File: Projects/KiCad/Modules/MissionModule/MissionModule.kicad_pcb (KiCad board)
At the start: 2 copper layers, 110 x 95 mm, 55 parts, among them J1 Conn_01x08, J2 Micro_SD_Card_Det_Hirose_DM3AT, SW1 SW_DIP_x02, U1 MCP2562-E-P, U2 MCP2515-I/P, U3 NJM7805SDL1, U5 TLP222A, U6 ABX00012, U7 MB85RS2MT, U8 MB85RS2MT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

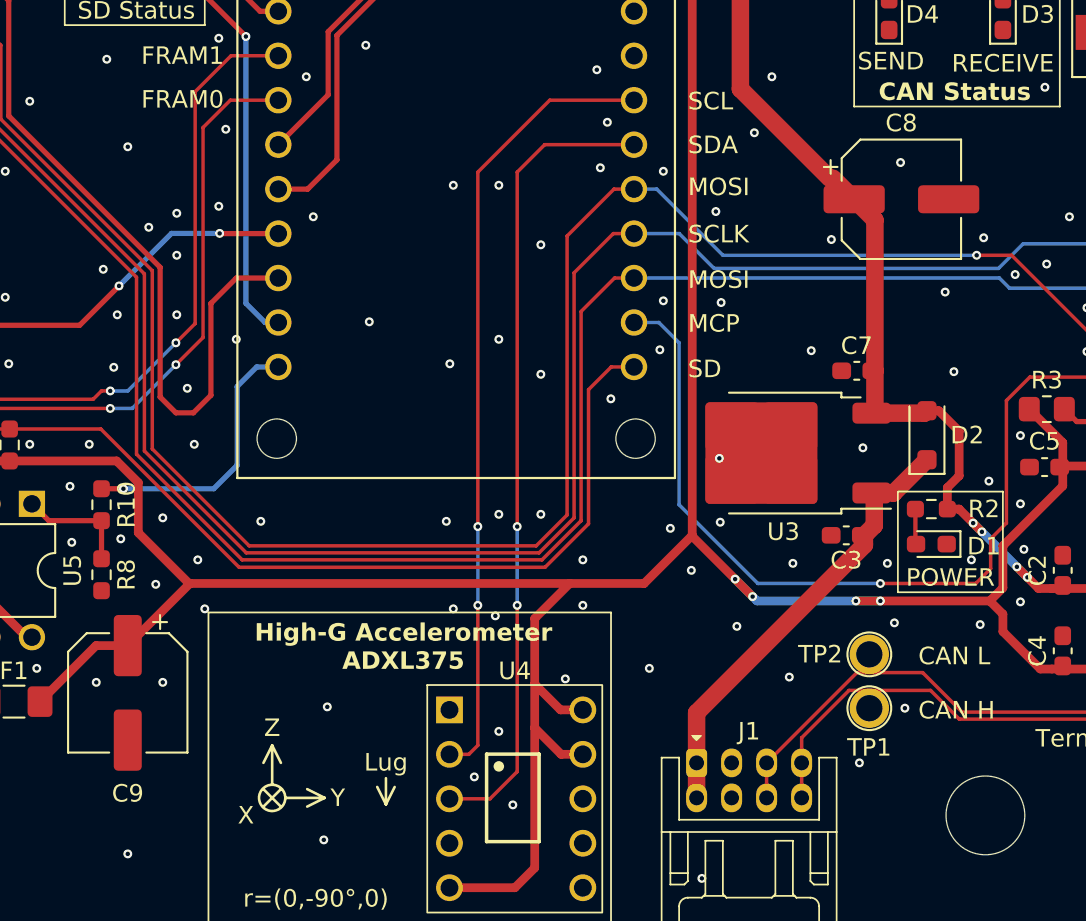
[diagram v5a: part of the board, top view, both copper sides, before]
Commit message: バッファコンデンサを表面実装に変更
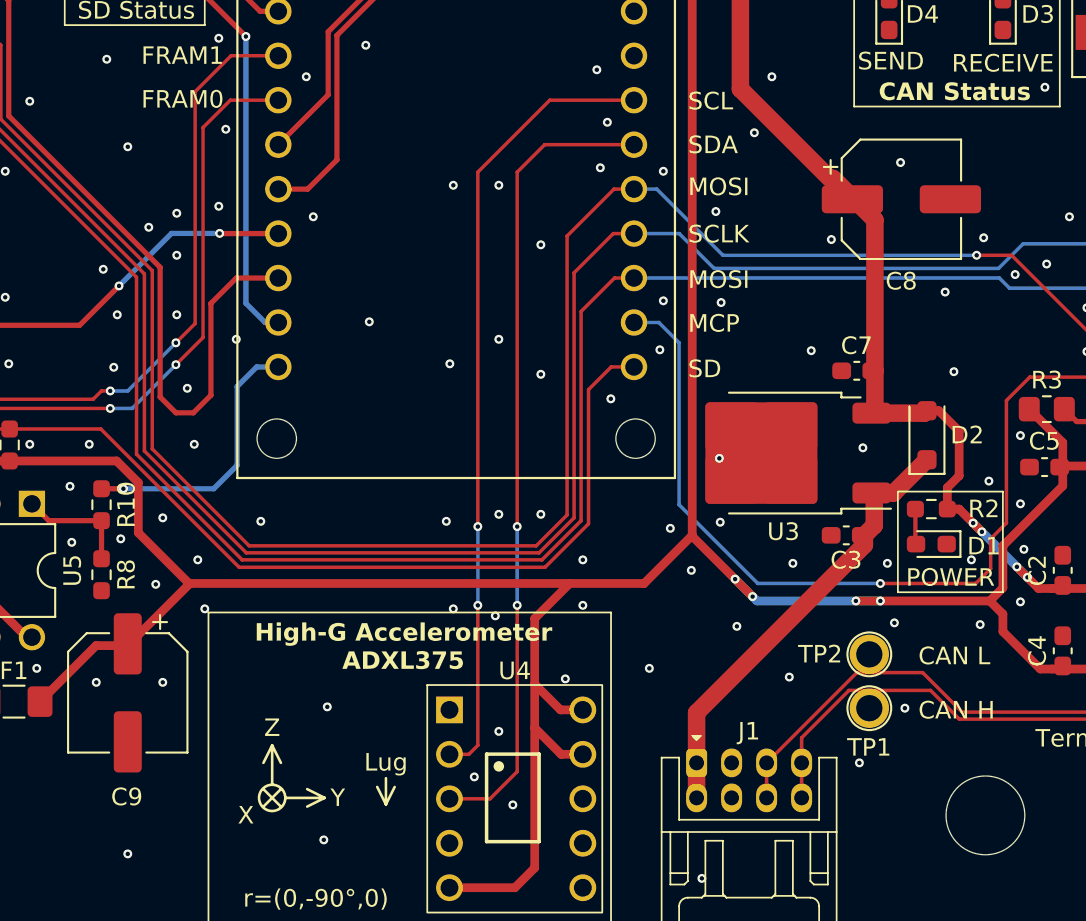
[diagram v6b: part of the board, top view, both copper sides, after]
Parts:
- C8, C9: value 100μF -> 47μF; footprint Capacitor_SMD:CP_Elec_6.3x7.7 -> Capacitor_SMD:CP_Elec_6.3x5.9

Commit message: チェックよし（多分）
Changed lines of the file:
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@@
     (fp_line (start 1 0.625) (end -1 0.625)
       (stroke (width 0.1) (type solid)) (layer "F.Fab"))
-    (pad "1" smd roundrect (at -1 0 270) (size 1.2 1.4) (layers "F.Cu" "F.Paste" "F.Mask") (roundrect_rratio 0.208333)
+    (pad "1" smd roundrect (at -1 0 270) (size 1.2 1.4) (layers "F.Cu" "F.Paste" "F.Mask") (roundrect_rratio 0.2083333333)
       (net 59 "LORA_SEND_STATUS") (pintype "passive"))
-    (pad "2" smd roundrect (at 1 0 270) (size 1.2 1.4) (layers "F.Cu" "F.Paste" "F.Mask") (roundrect_rratio 0.208333)
+    (pad "2" smd roundrect (at 1 0 270) (size 1.2 1.4) (layers "F.Cu" "F.Paste" "F.Mask") (roundrect_rratio 0.2083333333)
       (net 55 "Net-(D6-A)") (pintype "passive"))
     (model "${KICAD6_3DMODEL_DIR}/Resistor_SMD.3dshapes/R_0805_2012Metric.wrl"
@@
     (fp_line (start 1 0.625) (end -1 0.625)
       (stroke (width 0.1) (type solid)) (layer "F.Fab"))
-    (pad "1" smd roundrect (at -1 0) (size 1.2 1.4) (layers "F.Cu" "F.Paste" "F.Mask") (roundrect_rratio 0.208333)
+    (pad "1" smd roundrect (at -1 0) (size 1.2 1.4) (layers "F.Cu" "F.Paste" "F.Mask") (roundrect_rratio 0.2083333333)
       (net 5 "+3.3V") (pintype "passive"))
-    (pad "2" smd roundrect (at 1 0) (size 1.2 1.4) (layers "F.Cu" "F.Paste" "F.Mask") (roundrect_rratio 0.208333)
+    (pad "2" smd roundrect (at 1 0) (size 1.2 1.4) (layers "F.Cu" "F.Paste" "F.Mask") (roundrect_rratio 0.2083333333)
       (net 25 "Net-(U2-~RESET)") (pintype "passive"))
     (model "${KICAD6_3DMODEL_DIR}/Resistor_SMD.3dshapes/R_0805_2012Metric.wrl"
@@
     (fp_line (start 1 0.625) (end -1 0.625)
       (stroke (width 0.1) (type solid)) (layer "F.Fab"))
-    (pad "1" smd roundrect (at -1 0 270) (size 1.2 1.4) (layers "F.Cu" "F.Paste" "F.Mask") (roundrect_rratio 0.208333)
+    (pad "1" smd roundrect (at -1 0 270) (size 1.2 1.4) (layers "F.Cu" "F.Paste" "F.Mask") (roundrect_rratio 0.2083333333)
       (net 58 "LORA_RECEIVE_STATUS") (pintype "passive"))
-    (pad "2" smd roundrect (at 1 0 270) (size 1.2 1.4) (layers "F.Cu" "F.Paste" "F.Mask") (roundrect_rratio 0.208333)
+    (pad "2" smd roundrect (at 1 0 270) (size 1.2 1.4) (layers "F.Cu" "F.Paste" "F.Mask") (roundrect_rratio 0.2083333333)
       (net 35 "Net-(D5-A)") (pintype "passive"))
     (model "${KICAD6_3DMODEL_DIR}/Resistor_SMD.3dshapes/R_0805_2012Metric.wrl"
@@
     (fp_line (start 1 0.625) (end -1 0.625)
       (stroke (width 0.1) (type solid)) (layer "F.Fab"))
-    (pad "1" smd roundrect (at -1 0 270) (size 1.2 1.4) (layers "F.Cu" "F.Paste" "F.Mask") (roundrect_rratio 0.208333)
+    (pad "1" smd roundrect (at -1 0 270) (size 1.2 1.4) (layers "F.Cu" "F.Paste" "F.Mask") (roundrect_rratio 0.2083333333)
       (net 40 "CAN_RECEIVE_STATUS") (pintype "passive"))
-    (pad "2" smd roundrect (at 1 0 270) (size 1.2 1.4) (layers "F.Cu" "F.Paste" "F.Mask") (roundrect_rratio 0.208333)
+    (pad "2" smd roundrect (at 1 0 270) (size 1.2 1.4) (layers "F.Cu" "F.Paste" "F.Mask") (roundrect_rratio 0.2083333333)
       (net 21 "Net-(D3-A)") (pintype "passive"))
     (model "${KICAD6_3DMODEL_DIR}/Resistor_SMD.3dshapes/R_0805_2012Metric.wrl"
@@
     (fp_line (start 1 0.625) (end -1 0.625)
       (stroke (width 0.1) (type solid)) (layer "F.Fab"))
-    (pad "1" smd roundrect (at -1 0 270) (size 1.2 1.4) (layers "F.Cu" "F.Paste" "F.Mask") (roundrect_rratio 0.208333)
+    (pad "1" smd roundrect (at -1 0 270) (size 1.2 1.4) (layers "F.Cu" "F.Paste" "F.Mask") (roundrect_rratio 0.2083333333)
       (net 41 "CAN_SEND_STATUS") (pintype "passive"))
-    (pad "2" smd roundrect (at 1 0 270) (size 1.2 1.4) (layers "F.Cu" "F.Paste" "F.Mask") (roundrect_rratio 0.208333)
+    (pad "2" smd roundrect (at 1 0 270) (size 1.2 1.4) (layers "F.Cu" "F.Paste" "F.Mask") (roundrect_rratio 0.2083333333)
       (net 24 "Net-(D4-A)") (pintype "passive"))
     (model "${KICAD6_3DMODEL_DIR}/Resistor_SMD.3dshapes/R_0805_2012Metric.wrl"

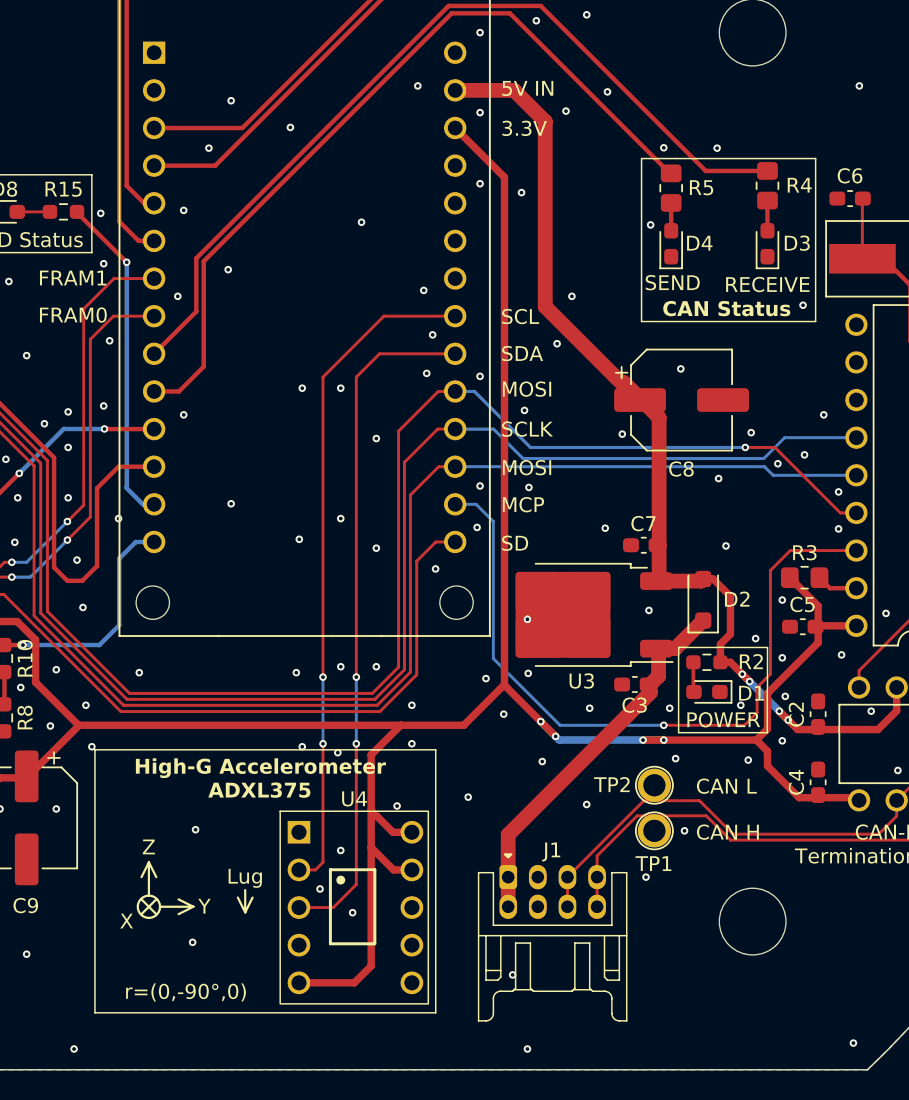
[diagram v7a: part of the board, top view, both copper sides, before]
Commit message: ADXLをSPI接続に変更
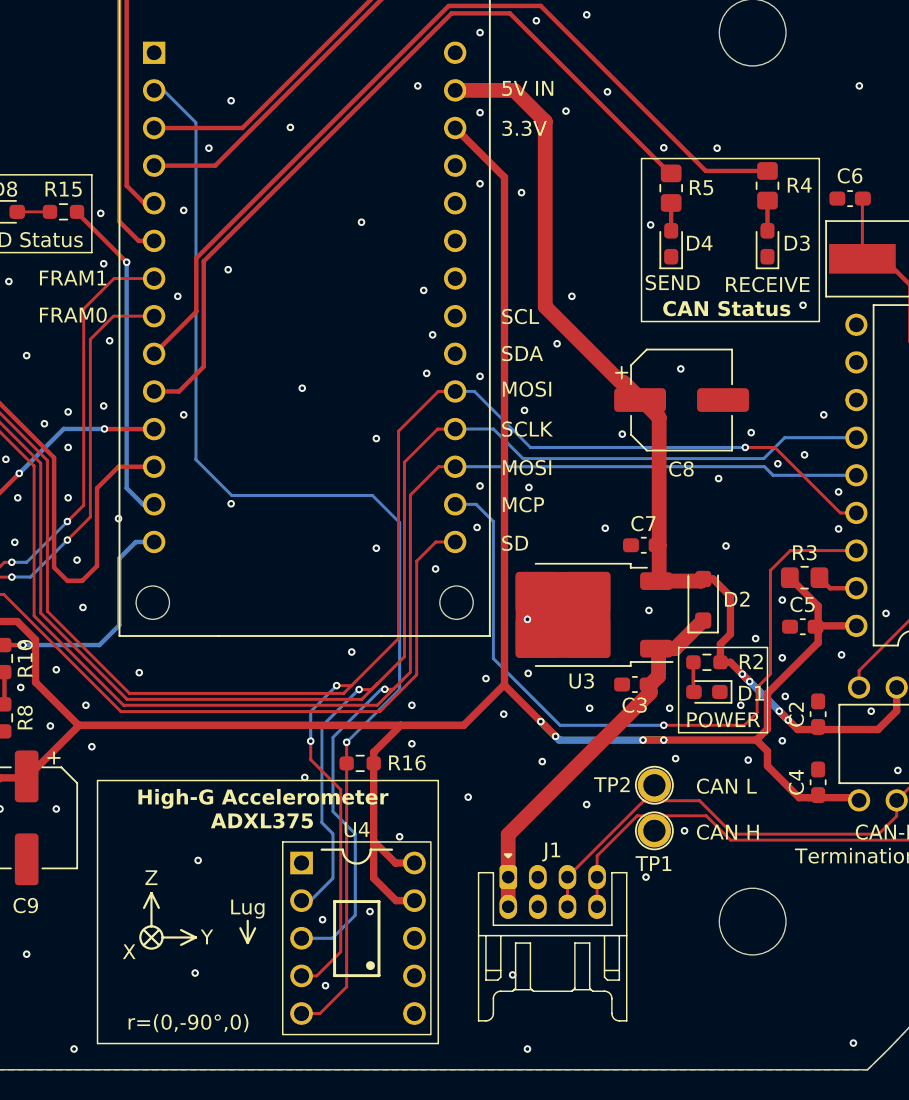
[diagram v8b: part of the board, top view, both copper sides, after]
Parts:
- added R16: 4.7kΩ, Resistor_SMD:R_0603_1608Metric_Pad0.98x0.95mm_HandSolder, F.Cu at (152.0, 124.3)
- moved U4 2.08 mm to (151.8, 129.6)
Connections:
- U4 pad 2: I2C_SCL -> SPI_SCLK
- U4 pad 3: I2C_SDA -> SPI_MOSI
- U4 pad 4: GND -> SPI_MISO
- U4 pad 5: +3.3V -> SPI_CS_ADXL
- U6 pad 2: unconnected-(U6-PA02_AIN0/DAC0/A0-Pad2) -> SPI_CS_ADXL
- U6 pad 20: I2C_SDA -> unconnected-(U6-PA08_S0_I2C_SDA-Pad20)
- U6 pad 21: I2C_SCL -> unconnected-(U6-PA09_S0_I2C_SCL-Pad21)
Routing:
- net SPI_CS_ADXL: track 0.00 -> 78.6 mm, vias 0 -> 1
- net I2C_SDA: track 46.1 -> 0.00 mm, vias 2 -> 0
- net I2C_SCL: track 45.2 -> 0.00 mm, vias 2 -> 0
- net SPI_MISO: track 154.2 -> 176.9 mm, vias 1 -> 3
- net SPI_MOSI: track 135.7 -> 158.3 mm, vias 1 -> 2
- net SPI_SCLK: track 147.9 -> 165.6 mm, vias 1 -> 2
- net +3.3V: track 176.6 -> 165.3 mm
- net GND: vias 187 -> 181
